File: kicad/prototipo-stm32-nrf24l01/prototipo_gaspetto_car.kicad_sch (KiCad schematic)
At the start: 18 parts, among them J1 Conn_01x07_Pin - TEST POINT, J2 NRF24L01_connector, J3 2x L911S connector, J4 Screw_Terminal_01x20, J5 Screw_Terminal_01x20, J6 Conn_01x04_Pin, M1 Motor_DC Right, M2 Motor_DC, Q1 BC548, U1 YAAJ_BluePill_Part_Like_SWD_B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

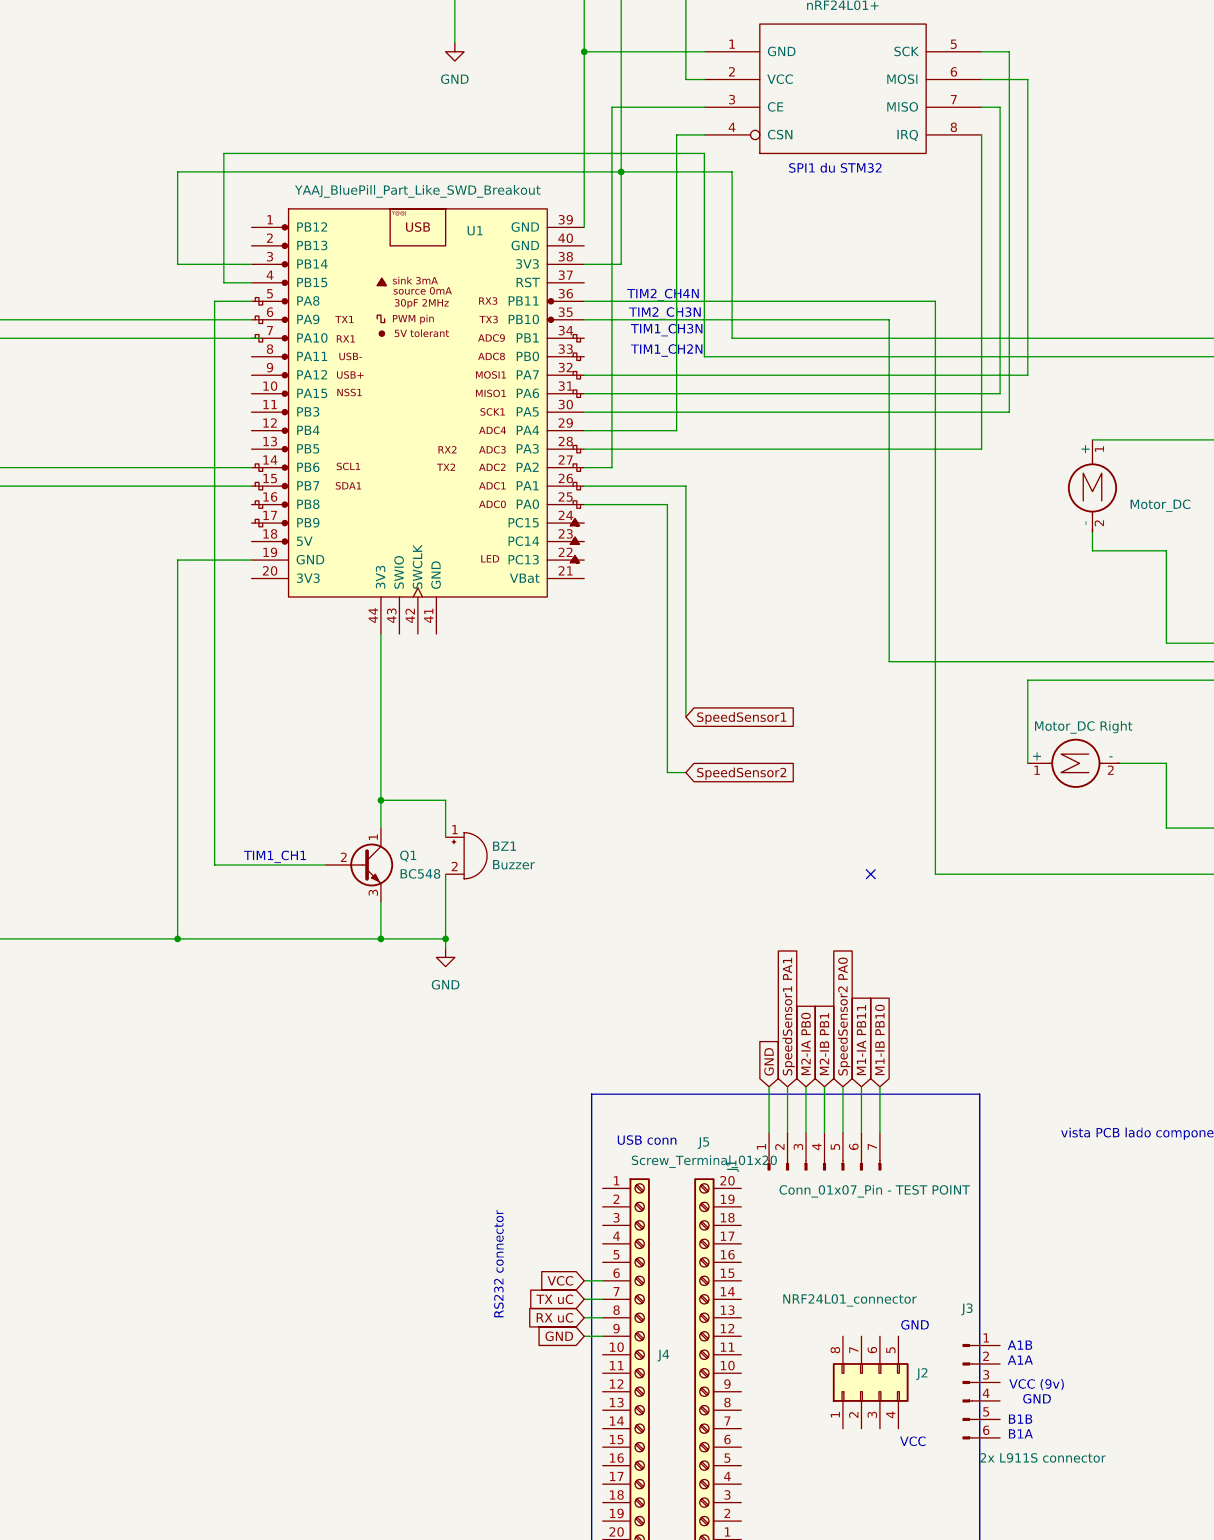
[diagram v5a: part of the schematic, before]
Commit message: good gpio pinout labels for motor
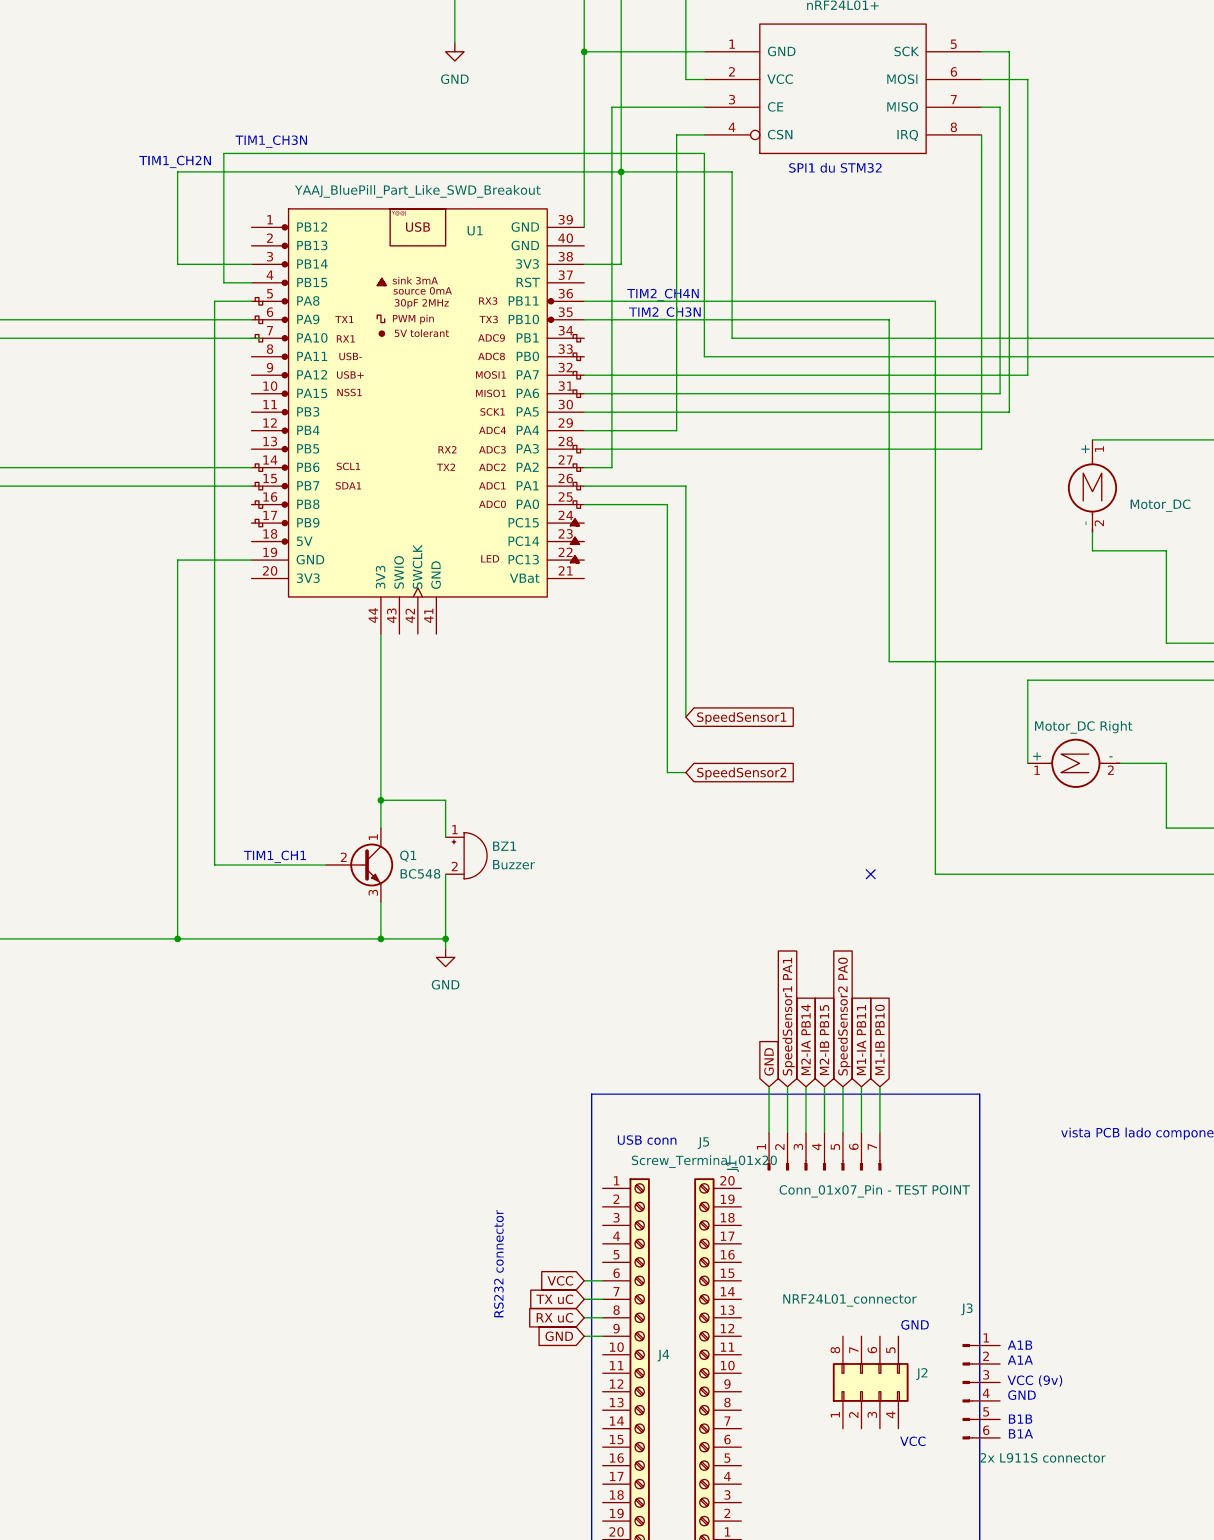
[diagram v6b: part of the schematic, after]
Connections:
- net M2-IA  PB0 renamed M2-IA  PB14
- net M2-IB  PB1 renamed M2-IB  PB15
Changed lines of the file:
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@@
 	(text "VCC (9v)\nGND"
 		(exclude_from_sim no)
-		(at 260.35 261.874 0)
-		(effects
-			(font
-				(size 1.27 1.27)
-			)
+		(at 256.286 261.366 0)
+		(effects
+			(font
+				(size 1.27 1.27)
+			)
+			(justify left)
 		)
 	)
@@
 	(text "TIM1_CH2N"
 		(exclude_from_sim no)
-		(at 209.55 118.618 0)
+		(at 141.986 92.71 0)
 		(effects
 			(font
@@
 	(text "TIM1_CH3N"
 		(exclude_from_sim no)
-		(at 209.55 115.824 0)
+		(at 155.194 89.916 0)
 		(effects
 			(font
@@
 		)
 	)
-	(global_label "M2-IB  PB1"
+	(global_label "M2-IB  PB15"
 		(shape input)
 		(at 231.14 219.71 90)
@@
 		)
 		(property "Intersheetrefs" "${INTERSHEET_REFS}"
-			(at 231.14 204.932 90)
+			(at 231.14 203.7225 90)
 			(effects
 				(font
@@
 		)
 	)
-	(global_label "M2-IA  PB0"
+	(global_label "M2-IA  PB14"
 		(shape input)
 		(at 228.6 219.71 90)
@@
 		)
 		(property "Intersheetrefs" "${INTERSHEET_REFS}"
-			(at 228.6 205.1134 90)
+			(at 228.6 203.9039 90)
 			(effects
 				(font

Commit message: sch: add new connections on blakcpill
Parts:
- added μC1: BlackPill, symbol muControllers_other:BlackPill
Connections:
- net at U1.28 (PA3): no longer U2.8 (IRQ)
- net SpeedSensor1: no longer names the net of U1.26 (PA1)
- net SpeedSensor1 PA1: no longer names the net of J1.2 (Pin_2)
- net SpeedSensor2: no longer names the net of U1.25 (PA0)
- net SpeedSensor2 PA0: no longer names the net of J1.5 (Pin_5)
- no-connect marks 1 -> 2
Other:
- note added: "ALT RX uC"
- note added: "ALT TX uC"
- note added: "Buzzer - T4_CH4 (16 bit counter for PWM)"
- note added: "CE"
- note added: "CSN"
- note added: "MISO"
- note added: "MOSI"
- note added: "PA1 blackpill"
- note added: "PA3 blackpill"
- note added: "SCK"
- note added: "SCL1 I2C MPU"
- note added: "SDA1 I2C MPU"
- note added: "T2_CH1"
- note added: "T2_CH2"
- note added: "T2_CH3"
- note added: "T2_CH4"
- note added: "csn"
- note added: "ok"
- note added: "~RX uC 1~"
- note added: "~TX uC 1~"
- moved on the sheet: J1, J2, J3, J4, J5
